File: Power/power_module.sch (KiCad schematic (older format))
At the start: 51 parts, among them J1 Conn_02x03_Odd_Even, J2 Conn_02x03_Odd_Even, J3 Conn_02x06_Counter_Clockwise, J4 Conn_02x05_Top_Bottom, J5 Conn_02x05_Top_Bottom, J6 Conn_02x02_Odd_Even, J7 Conn_02x02_Odd_Even, P3 CONN_01X04, P6 CONN_01X04, Q1 Q_NMOS_GDS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

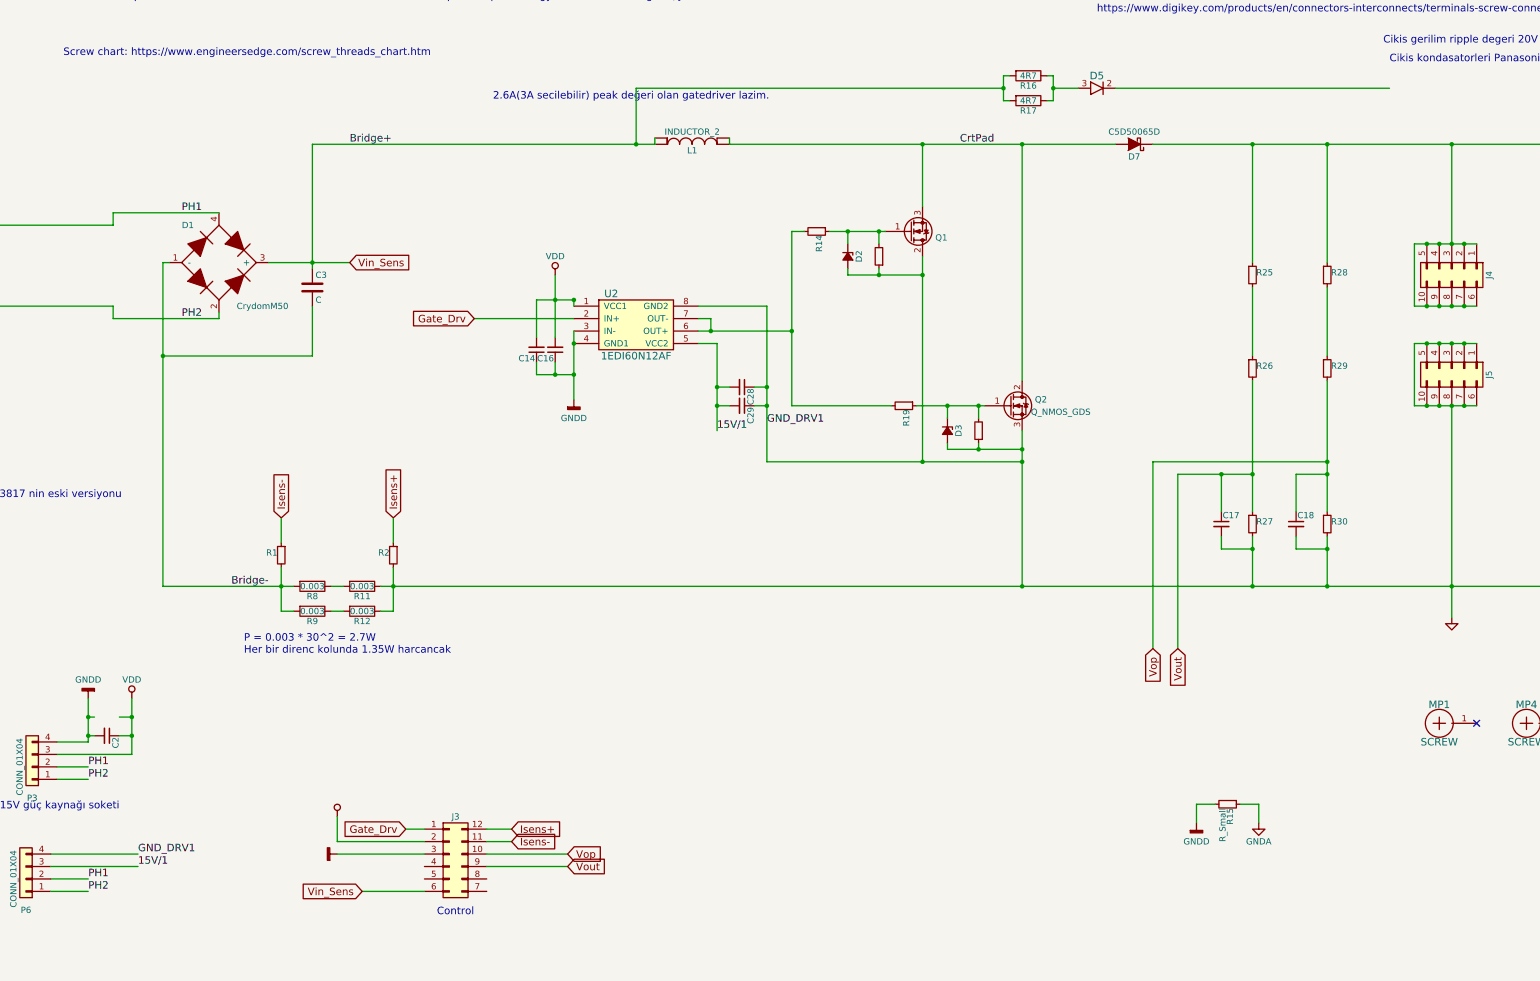
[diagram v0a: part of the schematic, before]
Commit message: Mevcut yerlesime gore kaba cizim yapildi.
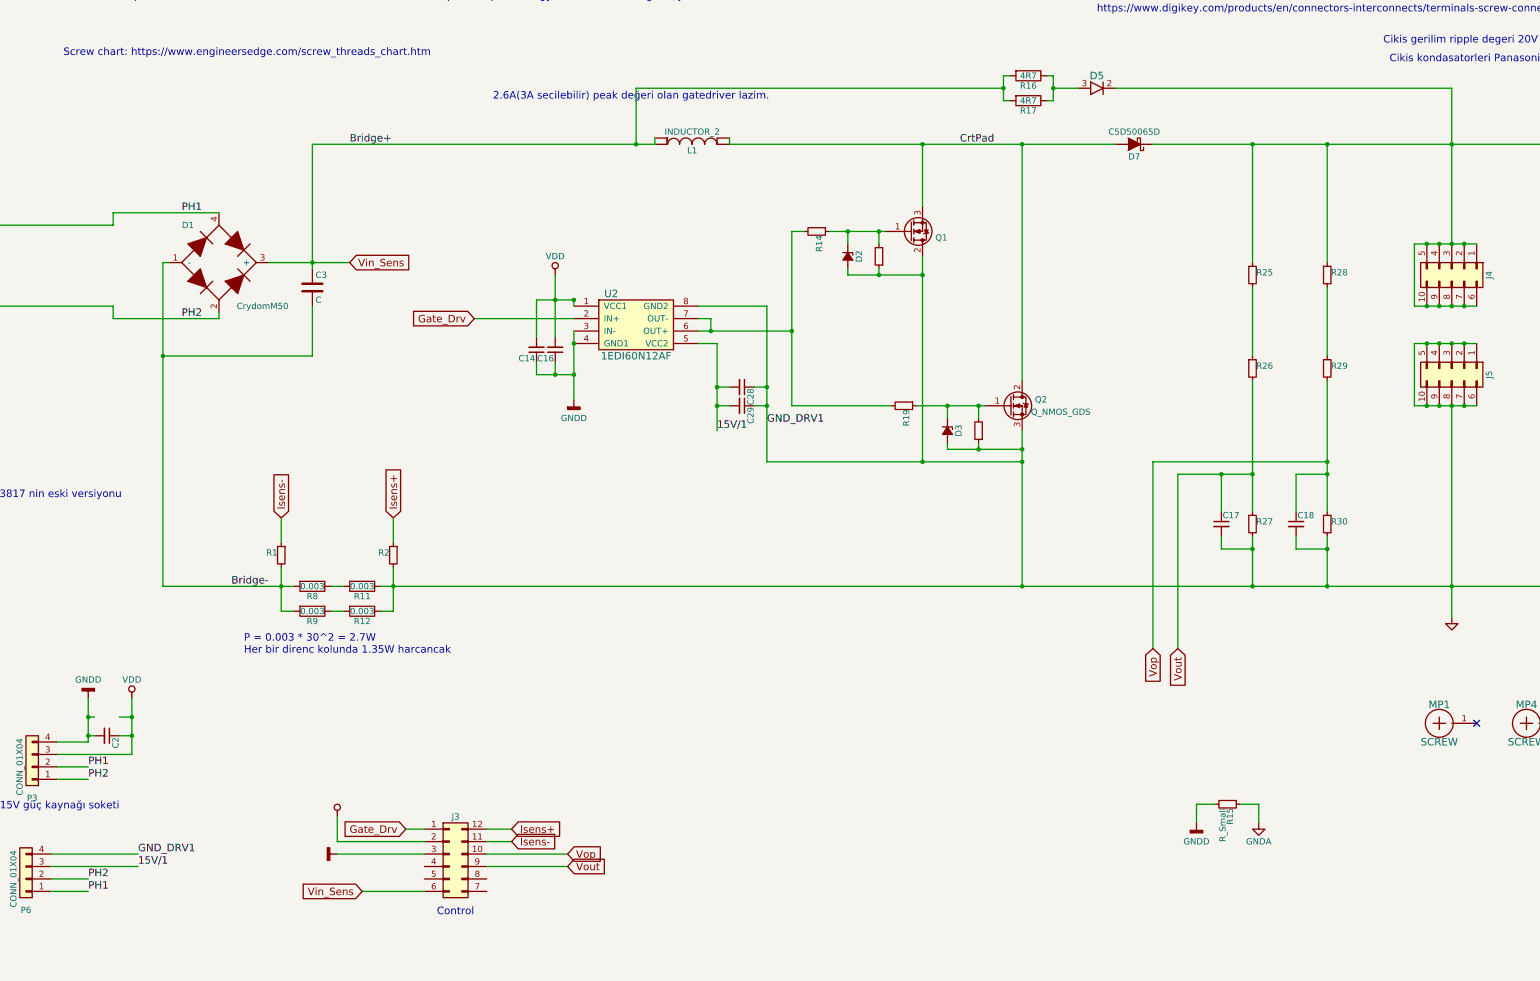
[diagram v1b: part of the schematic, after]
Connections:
- net PH1: now also P6.1 (Pin_1); no longer P6.2 (Pin_2)
- net PH2: now also P6.2 (Pin_2); no longer P6.1 (Pin_1)
- net Vout+: now also D5.2
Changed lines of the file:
@@
 Wire Wire Line
 	1800 7700 2500 7700
+Text Label 2100 7900 0    60   ~ 0
+PH2
 Text Label 2100 8000 0    60   ~ 0
-PH2
-Text Label 2100 7900 0    60   ~ 0
 PH1
 Wire Wire Line
@@
 Wire Wire Line
 	10050 1550 9850 1550
-Wire Wire Line
-	12550 1550 10350 1550
 Wire Wire Line
 	1000 2150 1350 2150
@@
 	13950 4200 14450 4200
 Wire Wire Line
-	13050 2800 13050 2000
+	13050 1550 13050 2800
 Connection ~ 13050 2000
 Wire Wire Line
@@
 Wire Wire Line
 	4100 7700 4800 7700
+Wire Wire Line
+	10350 1550 13050 1550
 $EndSCHEMATC
